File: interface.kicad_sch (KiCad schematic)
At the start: 9 parts

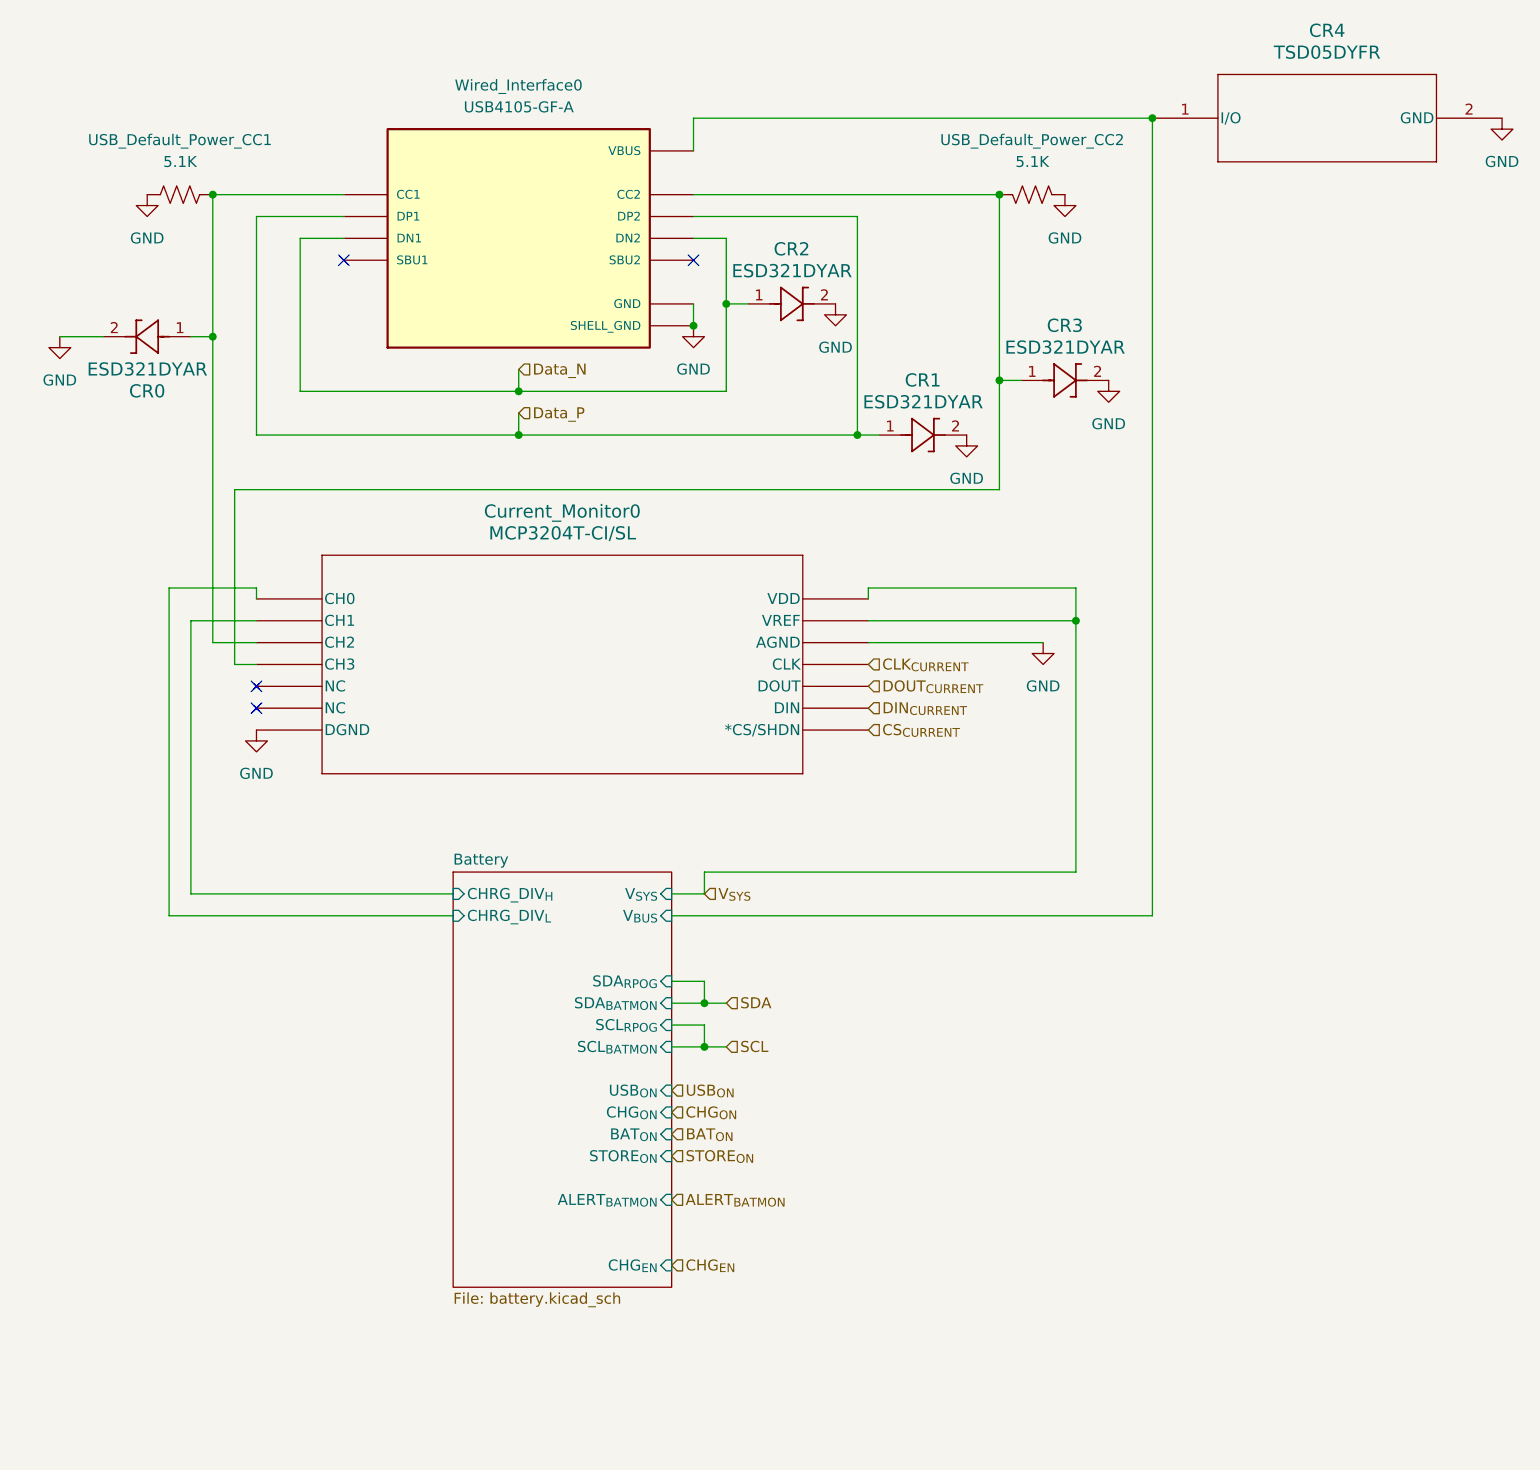
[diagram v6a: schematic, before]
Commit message: Replace USB connector
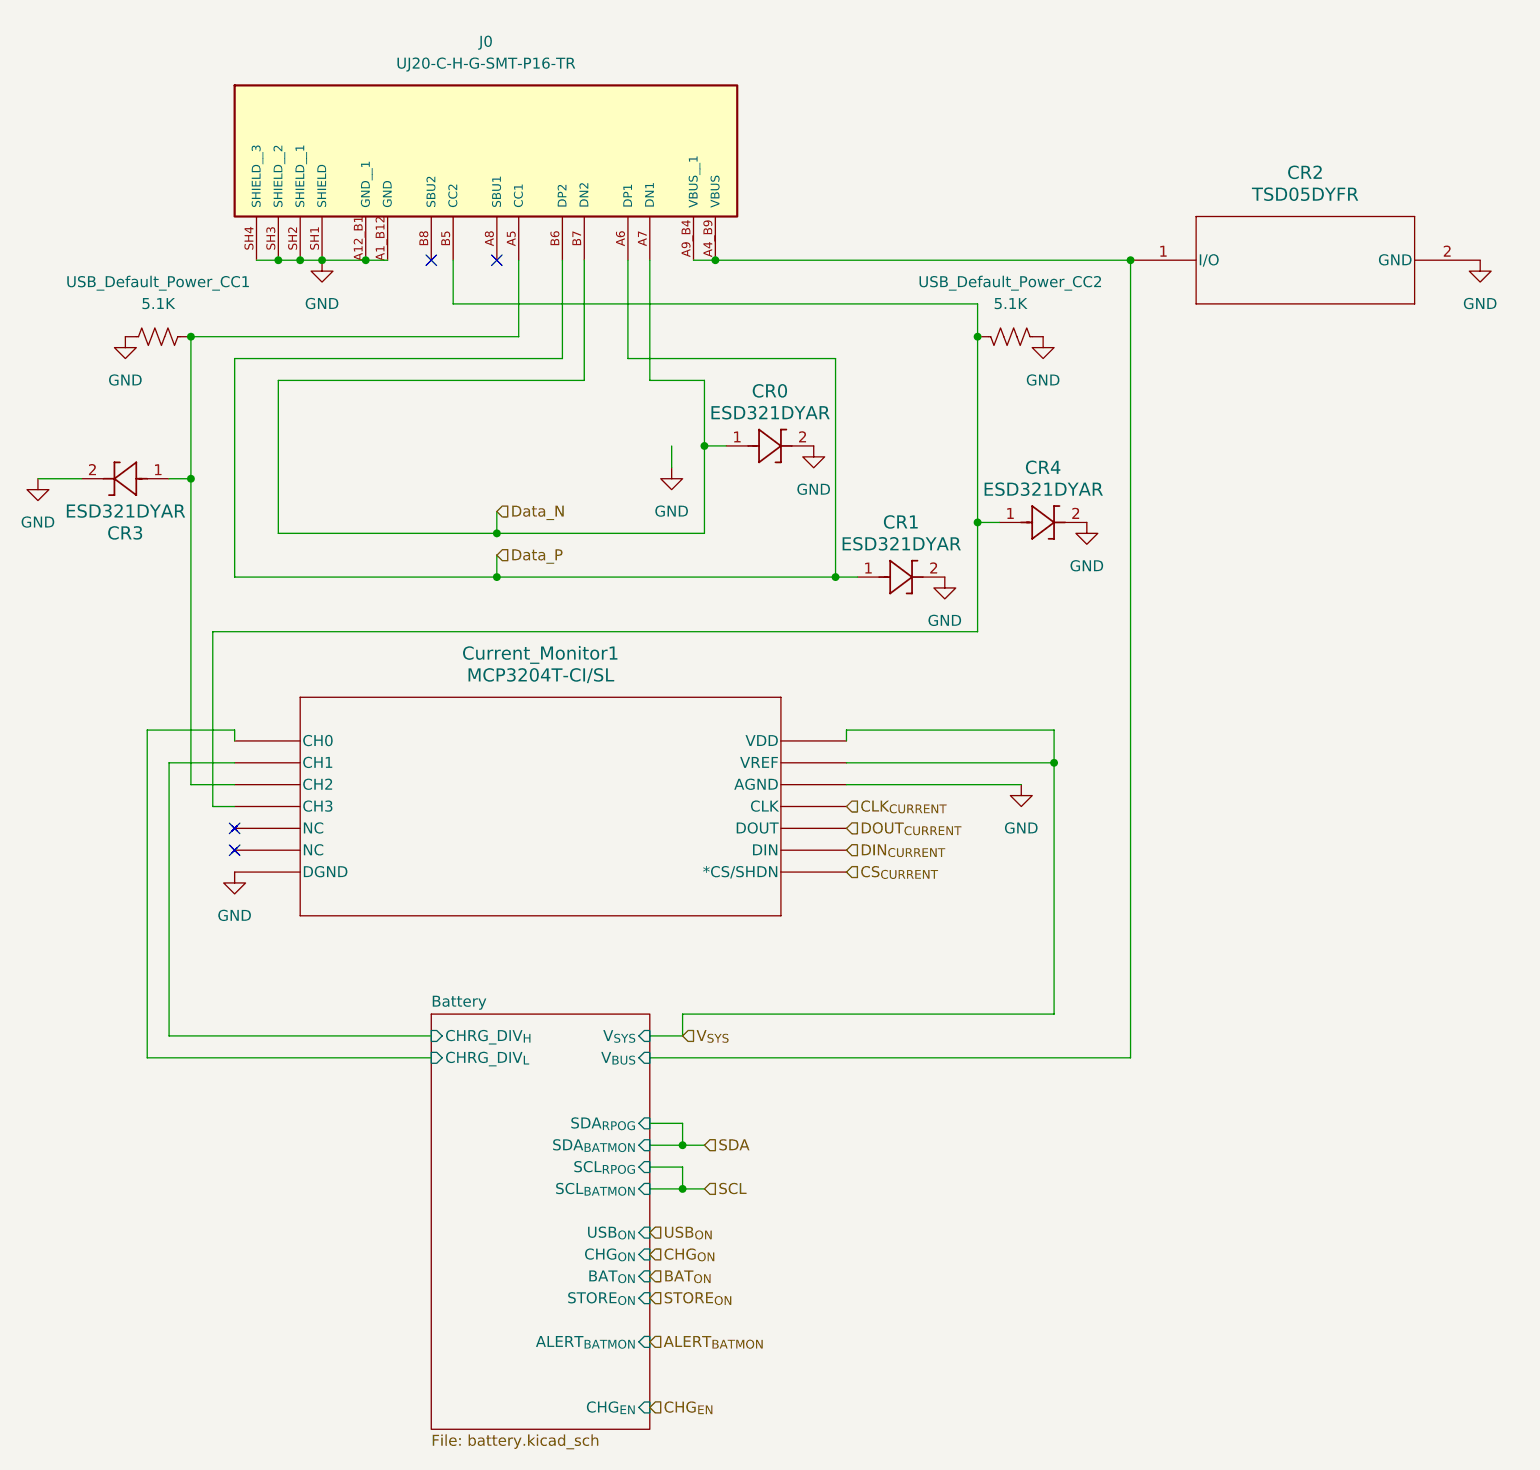
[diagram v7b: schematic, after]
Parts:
- removed Wired_Interface0: USB4105-GF-A, GCT_USB4105-GF-A, symbol USB4105-GF-A:USB4105-GF-A
- added J0: UJ20-C-H-G-SMT-P16-TR, snap_magic_footprints:SAMESKY_UJ20-C-H-G-SMT-P16-TR, symbol UJ20-C-H-G-SMT-P16-TR:UJ20-C-H-G-SMT-P16-TR
- renumbered CR2 to CR0, CR4 to CR2, CR0 to CR3, CR3 to CR4, Current_Monitor0 to Current_Monitor1
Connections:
- net Battery/V_{BUS}: now also J0.A4_B9 (VBUS), J0.A9_B4 (VBUS__1)
- net Data_N: now also J0.A7 (DN1), J0.B7 (DN2)
- net Data_P: now also J0.A6 (DP1), J0.B6 (DP2)
- net GND: now also J0.A12_B1 (GND__1), J0.A1_B12 (GND), J0.SH1 (SHIELD), J0.SH2 (SHIELD__1), J0.SH3 (SHIELD__2), J0.SH4 (SHIELD__3)
- net at CR3.1, Current_Monitor1.3 (CH2), USB_Default_Power_CC1.1: now also J0.A5 (CC1)
- net at CR4.1, Current_Monitor1.4 (CH3), USB_Default_Power_CC2.1: now also J0.B5 (CC2)
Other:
- moved on the sheet: CR0, CR1, CR2, CR3, CR4, Current_Monitor1, USB_Default_Power_CC1, USB_Default_Power_CC2

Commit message: Update layout
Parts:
- J0: footprint snap_magic_footprints:SAMESKY_UJ20-C-H-G-SMT-P16-TR -> UJ20-C-H-G-SMT-P16-TR:SAMESKY_UJ20-C-H-G-SMT-P16-TR
- renumbered CR3 to CR0, CR0 to CR2, CR4 to CR3, CR2 to CR4, Current_Monitor1 to Current_Monitor0, USB_Default_Power_CC2 to USB_Default_Power_CC1, USB_Default_Power_CC1 to USB_Default_Power_CC2
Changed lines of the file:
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@@
+	)
+	(junction
+		(at 124.46 48.26)
+		(diameter 0)
+		(color 0 0 0 0)
 	)
 	(junction
@@
 	(wire
 		(pts
-			(xy 162.56 69.85) (xy 162.56 72.39)
-		)
-		(stroke
-			(width 0)
-			(type default)
-		)
-	)
-	(wire
-		(pts
 			(xy 111.76 111.76) (xy 109.22 111.76)
 		)
@@
 	(wire
 		(pts
+			(xy 124.46 48.26) (xy 121.92 48.26)
+		)
+		(stroke
+			(width 0)
+			(type default)
+		)
+	)
+	(wire
+		(pts
 			(xy 167.64 48.26) (xy 215.9 48.26)
 		)
@@
 	(wire
 		(pts
-			(xy 121.92 48.26) (xy 127 48.26)
-		)
-		(stroke
-			(width 0)
-			(type default)
-		)
-	)
-	(wire
-		(pts
 			(xy 104.14 73.66) (xy 106.68 73.66)
 		)
@@
 		(pts
 			(xy 160.02 138.43) (xy 163.83 138.43)
+		)
+		(stroke
+			(width 0)
+			(type default)
+		)
+	)
+	(wire
+		(pts
+			(xy 124.46 48.26) (xy 127 48.26)
 		)
 		(stroke
@@
 		(dnp no)
 		(fields_autoplaced yes)
-		(property "Reference" "#PWR09"
+		(property "Reference" "#PWR07"
 			(at 179.07 76.2 0)
 			(effects
@@
 		(dnp no)
 		(fields_autoplaced yes)
-		(property "Reference" "USB_Default_Power_CC1"
+		(property "Reference" "USB_Default_Power_CC2"
 			(at 102.87 50.8 90)
 			(effects
@@
 		(dnp no)
 		(fields_autoplaced yes)
-		(property "Reference" "#PWR023"
+		(property "Reference" "#PWR037"
 			(at 256.54 54.61 0)
 			(effects
@@
 		(dnp no)
 		(fields_autoplaced yes)
-		(property "Reference" "#PWR021"
+		(property "Reference" "#PWR08"
 			(at 194.31 91.44 0)
 			(effects
@@
 		(dnp no)
 		(fields_autoplaced yes)
-		(property "Reference" "#PWR027"
+		(property "Reference" "#PWR035"
 			(at 88.9 80.01 0)
 			(effects
@@
 		(dnp no)
 		(fields_autoplaced yes)
-		(property "Reference" "CR3"
+		(property "Reference" "CR0"
 			(at 99.06 80.01 0)
 			(effects
@@
 		(dnp no)
 		(fields_autoplaced yes)
-		(property "Reference" "#PWR0105"
+		(property "Reference" "#PWR04"
 			(at 111.76 125.73 0)
 			(effects
@@
 				(path "/efcccfe8-5e20-4b1b-8d3b-61fce771481e/cd3314d0-f605-42f0-be2b-644cabc7637c"
 					(reference "#PWR0105")
-					(unit 1)
-				)
-			)
-		)
-	)
-	(symbol
-		(lib_id "power:GND")
-		(at 162.56 72.39 0)
-		(unit 1)
-		(exclude_from_sim no)
-		(in_bom yes)
-		(on_board yes)
-		(dnp no)
-		(fields_autoplaced yes)
-		(property "Reference" "#PWR0103"
-			(at 162.56 78.74 0)
-			(effects
-				(font
-					(size 1.27 1.27)
-				)
-				(hide yes)
-			)
-		)
-		(property "Value" "GND"
-			(at 162.56 77.47 0)
-			(effects
-				(font
-					(size 1.27 1.27)
-				)
-			)
-		)
-		(property "Footprint" ""
-			(at 162.56 72.39 0)
-			(effects
-				(font
-					(size 1.27 1.27)
-				)
-				(hide yes)
-			)
-		)
-		(property "Datasheet" ""
-			(at 162.56 72.39 0)
-			(effects
-				(font
-					(size 1.27 1.27)
-				)
-				(hide yes)
-			)
-		)
-		(property "Description" "Power symbol creates a global label with name \"GND\" , ground"
-			(at 162.56 72.39 0)
-			(effects
-				(font
-					(size 1.27 1.27)
-				)
-				(hide yes)
-			)
-		)
-		(pin "1"
-		)
-		(instances
-			(project "portable_steno"
-				(path "/06a6eca0-edda-4cc0-a23f-017602e67f07/99f3b279-b2b0-4dd5-ab05-9b518546ce95/cd3314d0-f605-42f0-be2b-644cabc7637c"
-					(reference "#PWR01")
-					(unit 1)
-				)
-			)
-			(project "right_hand"
-				(path "/efcccfe8-5e20-4b1b-8d3b-61fce771481e/cd3314d0-f605-42f0-be2b-644cabc7637c"
-					(reference "#PWR0103")
 					(unit 1)
 				)
@@
 		(dnp no)
 		(fields_autoplaced yes)
-		(property "Reference" "CR2"
+		(property "Reference" "CR4"
 			(at 236.22 38.1 0)
 			(effects
@@
 		(on_board yes)
 		(dnp no)
-		(property "Reference" "Current_Monitor1"
+		(property "Reference" "Current_Monitor0"
 			(at 147.32 93.98 0)
 			(effects
@@
 		(dnp no)
 		(fields_autoplaced yes)
-		(property "Reference" "#PWR0101"
+		(property "Reference" "#PWR03"
 			(at 205.74 63.5 0)
 			(effects
@@
 		(dnp no)
 		(fields_autoplaced yes)
-		(property "Reference" "CR4"
+		(property "Reference" "CR3"
 			(at 205.74 72.39 0)
 			(effects
@@
 		(dnp no)
 		(fields_autoplaced yes)
-		(property "Reference" "#PWR0102"
+		(property "Reference" "#PWR05"
 			(at 203.2 115.57 0)
 			(effects
@@
 	(symbol
 		(lib_id "power:GND")
-		(at 121.92 48.26 0)
+		(at 124.46 48.26 0)
 		(unit 1)
 		(exclude_from_sim no)
@@
 		(dnp no)
 		(fields_autoplaced yes)
-		(property "Reference" "#PWR0106"
-			(at 121.92 54.61 0)
+		(property "Reference" "#PWR0104"
+			(at 124.46 54.61 0)
 			(effects
 				(font
@@
 		)
 		(property "Value" "GND"
-			(at 121.92 53.34 0)
+			(at 124.46 53.34 0)
 			(effects
 				(font
@@
 		)
 		(property "Footprint" ""
-			(at 121.92 48.26 0)
+			(at 124.46 48.26 0)
 			(effects
 				(font
@@
 		)
 		(property "Datasheet" ""
-			(at 121.92 48.26 0)
+			(at 124.46 48.26 0)
 			(effects
 				(font
@@
 		)
 		(property "Description" "Power symbol creates a global label with name \"GND\" , ground"
-			(at 121.92 48.26 0)
+			(at 124.46 48.26 0)
 			(effects
 				(font
@@
 		(dnp no)
 		(fields_autoplaced yes)
-		(property "Reference" "#PWR0104"
+		(property "Reference" "#PWR02"
 			(at 99.06 63.5 0)
 			(effects
@@
 		(dnp no)
 		(fields_autoplaced yes)
-		(property "Reference" "CR0"
+		(property "Reference" "CR2"
 			(at 173.99 63.5 0)
 			(effects
@@
 			)
 		)
-		(property "Footprint" "snap_magic_footprints:SAMESKY_UJ20-C-H-G-SMT-P16-TR"
+		(property "Footprint" "UJ20-C-H-G-SMT-P16-TR:SAMESKY_UJ20-C-H-G-SMT-P16-TR"
 			(at 147.32 35.56 0)
 			(effects
@@
 		(dnp no)
 		(fields_autoplaced yes)
-		(property "Reference" "#PWR028"
+		(property "Reference" "#PWR036"
 			(at 210.82 85.09 0)
 			(effects
@@
 		(dnp no)
 		(fields_autoplaced yes)
-		(property "Reference" "USB_Default_Power_CC2"
+		(property "Reference" "USB_Default_Power_CC1"
 			(at 201.93 50.8 90)
 			(effects
